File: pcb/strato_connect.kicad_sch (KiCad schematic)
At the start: 44 parts, among them J1 Conn_Coaxial, J2 Conn_01x04_Pin, J3 Conn_01x04_Pin, J5 Conn_01x01_Pin, J6 Conn_01x02_Pin, SW1 SW_SPST, U1 TPS565242, U2 ATmega328PB-M, U4 RF4463F30, Y1 CSTNE16M0V530000R0

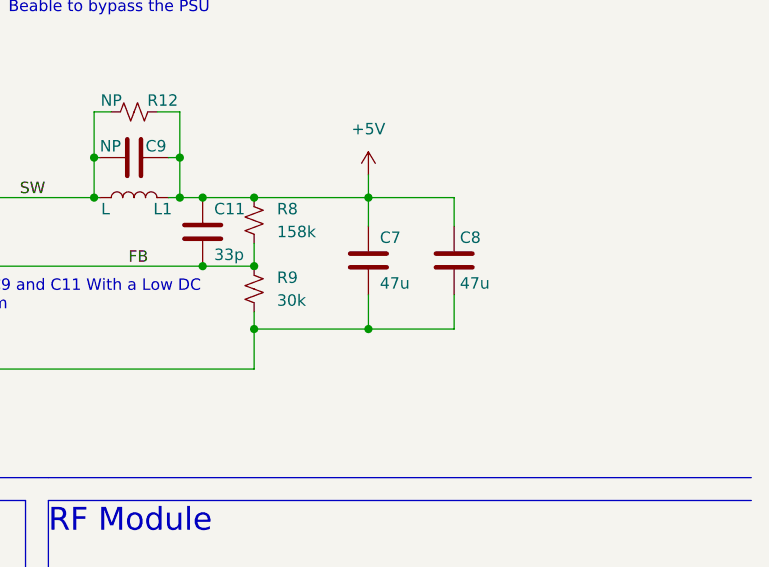
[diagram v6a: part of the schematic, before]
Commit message: add v2 files for the pcb, add the base code directory
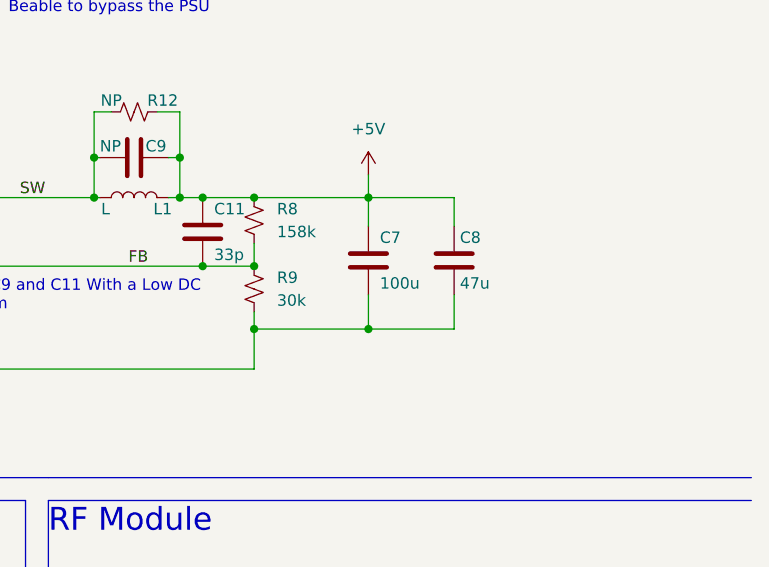
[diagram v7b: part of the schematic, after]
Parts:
- C7: value 47u -> 100u
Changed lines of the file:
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@@
       (effects (font (size 1.27 1.27)) (justify left))
     )
-    (property "Value" "47u" (at 243.84 59.055 0)
+    (property "Value" "100u" (at 243.84 59.055 0)
       (effects (font (size 1.27 1.27)) (justify left))
     )
